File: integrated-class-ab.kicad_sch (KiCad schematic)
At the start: 1 part, among them U7 LT1794

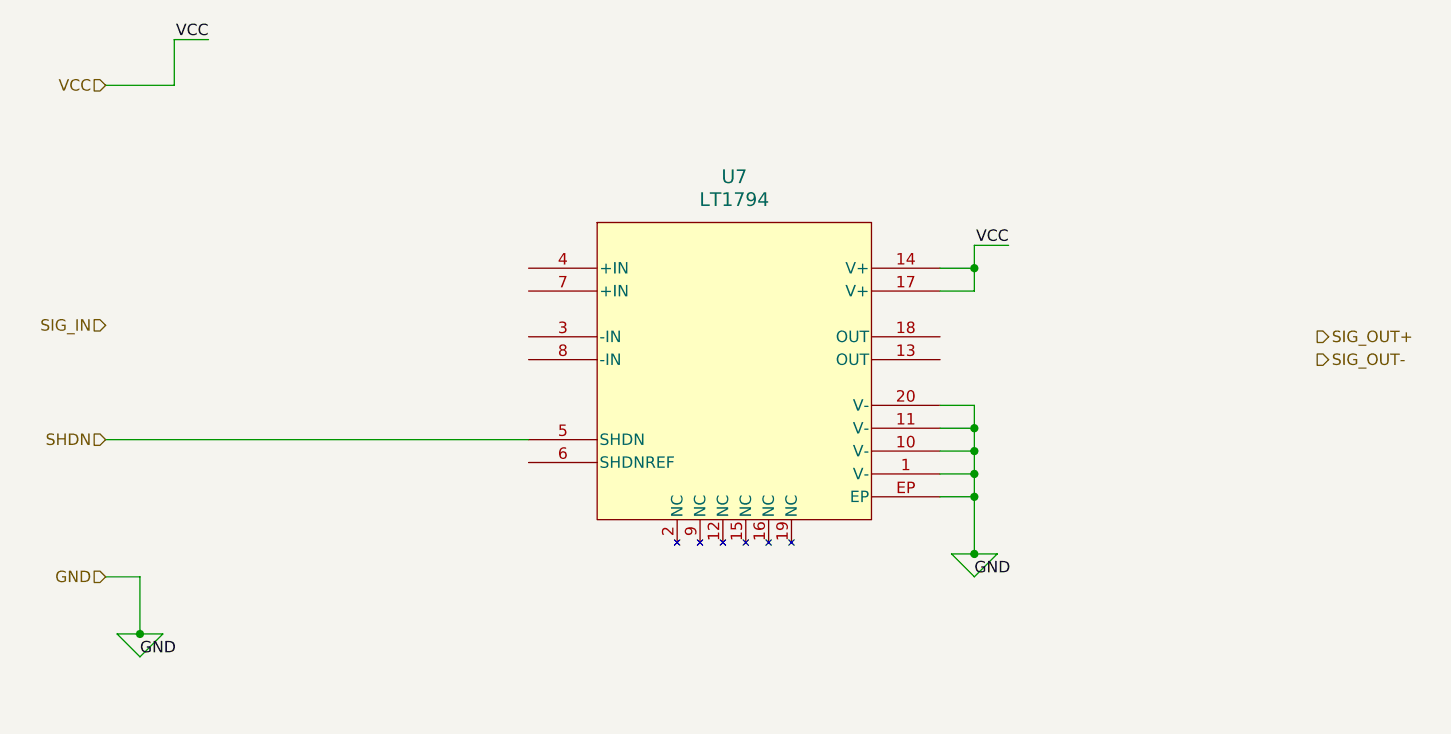
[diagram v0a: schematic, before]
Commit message: Added the pin headers to TX, working on a HV line driver design
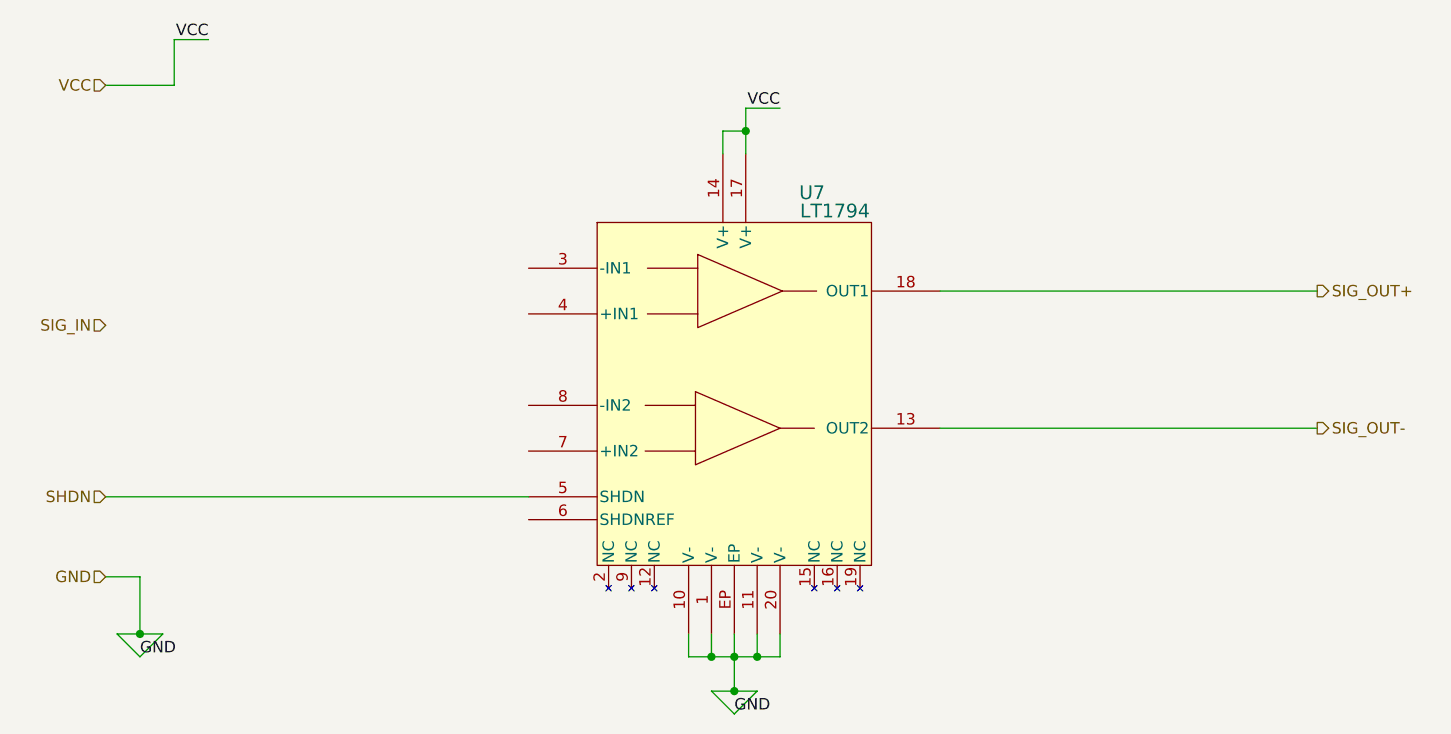
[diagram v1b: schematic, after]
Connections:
- net SIG_OUT+: now also U7.18 (OUT1)
- net SIG_OUT-: now also U7.13 (OUT2)
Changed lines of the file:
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@@
 	(paper "A4")
 	(junction
-		(at 176.53 96.52)
-		(diameter 0)
-		(color 0 0 0 0)
-	)
-	(junction
-		(at 176.53 102.87)
-		(diameter 0)
-		(color 0 0 0 0)
-	)
-	(junction
-		(at 176.53 93.98)
-		(diameter 0)
-		(color 0 0 0 0)
-	)
-	(junction
-		(at 176.53 91.44)
-		(diameter 0)
-		(color 0 0 0 0)
-	)
-	(junction
-		(at 176.53 88.9)
-		(diameter 0)
-		(color 0 0 0 0)
-	)
-	(junction
-		(at 176.53 71.12)
+		(at 147.32 114.3)
+		(diameter 0)
+		(color 0 0 0 0)
+	)
+	(junction
+		(at 149.86 118.11)
+		(diameter 0)
+		(color 0 0 0 0)
+	)
+	(junction
+		(at 149.86 114.3)
+		(diameter 0)
+		(color 0 0 0 0)
+	)
+	(junction
+		(at 151.13 55.88)
 		(diameter 0)
 		(color 0 0 0 0)
@@
 		(color 0 0 0 0)
 	)
-	(wire
-		(pts
-			(xy 176.53 96.52) (xy 172.72 96.52)
-		)
-		(stroke
-			(width 0)
-			(type default)
-		)
-	)
-	(wire
-		(pts
-			(xy 176.53 105.41) (xy 179.07 102.87)
+	(junction
+		(at 152.4 114.3)
+		(diameter 0)
+		(color 0 0 0 0)
+	)
+	(wire
+		(pts
+			(xy 144.78 111.76) (xy 144.78 114.3)
+		)
+		(stroke
+			(width 0)
+			(type default)
+		)
+	)
+	(wire
+		(pts
+			(xy 149.86 114.3) (xy 149.86 118.11)
+		)
+		(stroke
+			(width 0)
+			(type default)
+		)
+	)
+	(wire
+		(pts
+			(xy 149.86 120.65) (xy 152.4 118.11)
 		)
 		(stroke
@@
 	(wire
 		(pts
-			(xy 176.53 71.12) (xy 176.53 68.58)
+			(xy 151.13 55.88) (xy 151.13 53.34)
 		)
 		(stroke
@@
 	(wire
 		(pts
-			(xy 176.53 102.87) (xy 179.07 102.87)
-		)
-		(stroke
-			(width 0)
-			(type default)
-		)
-	)
-	(wire
-		(pts
-			(xy 176.53 93.98) (xy 176.53 91.44)
-		)
-		(stroke
-			(width 0)
-			(type default)
-		)
-	)
-	(wire
-		(pts
-			(xy 176.53 88.9) (xy 176.53 86.36)
+			(xy 149.86 118.11) (xy 152.4 118.11)
 		)
 		(stroke
@@
 	(wire
 		(pts
+			(xy 149.86 114.3) (xy 152.4 114.3)
+		)
+		(stroke
+			(width 0)
+			(type default)
+		)
+	)
+	(wire
+		(pts
+			(xy 144.78 114.3) (xy 147.32 114.3)
+		)
+		(stroke
+			(width 0)
+			(type default)
+		)
+	)
+	(wire
+		(pts
 			(xy 83.82 111.76) (xy 86.36 111.76)
 		)
@@
 	(wire
 		(pts
-			(xy 172.72 93.98) (xy 176.53 93.98)
-		)
-		(stroke
-			(width 0)
-			(type default)
-		)
-	)
-	(wire
-		(pts
-			(xy 172.72 91.44) (xy 176.53 91.44)
-		)
-		(stroke
-			(width 0)
-			(type default)
-		)
-	)
-	(wire
-		(pts
-			(xy 172.72 86.36) (xy 176.53 86.36)
-		)
-		(stroke
-			(width 0)
-			(type default)
-		)
-	)
-	(wire
-		(pts
-			(xy 172.72 71.12) (xy 176.53 71.12)
-		)
-		(stroke
-			(width 0)
-			(type default)
-		)
-	)
-	(wire
-		(pts
-			(xy 176.53 73.66) (xy 176.53 71.12)
-		)
-		(stroke
-			(width 0)
-			(type default)
-		)
-	)
-	(wire
-		(pts
-			(xy 176.53 91.44) (xy 176.53 88.9)
-		)
-		(stroke
-			(width 0)
-			(type default)
-		)
-	)
-	(wire
-		(pts
-			(xy 176.53 68.58) (xy 180.34 68.58)
+			(xy 147.32 114.3) (xy 149.86 114.3)
+		)
+		(stroke
+			(width 0)
+			(type default)
+		)
+	)
+	(wire
+		(pts
+			(xy 147.32 111.76) (xy 147.32 114.3)
+		)
+		(stroke
+			(width 0)
+			(type default)
+		)
+	)
+	(wire
+		(pts
+			(xy 151.13 58.42) (xy 151.13 55.88)
+		)
+		(stroke
+			(width 0)
+			(type default)
+		)
+	)
+	(wire
+		(pts
+			(xy 148.59 55.88) (xy 148.59 58.42)
+		)
+		(stroke
+			(width 0)
+			(type default)
+		)
+	)
+	(wire
+		(pts
+			(xy 151.13 53.34) (xy 154.94 53.34)
 		)
 		(stroke
@@
 	(wire
 		(pts
-			(xy 173.99 102.87) (xy 176.53 102.87)
+			(xy 152.4 111.76) (xy 152.4 114.3)
+		)
+		(stroke
+			(width 0)
+			(type default)
+		)
+	)
+	(wire
+		(pts
+			(xy 154.94 114.3) (xy 154.94 111.76)
+		)
+		(stroke
+			(width 0)
+			(type default)
+		)
+	)
+	(wire
+		(pts
+			(xy 147.32 118.11) (xy 149.86 118.11)
 		)
 		(stroke
@@
 	(wire
 		(pts
-			(xy 176.53 96.52) (xy 176.53 93.98)
-		)
-		(stroke
-			(width 0)
-			(type default)
-		)
-	)
-	(wire
-		(pts
-			(xy 176.53 96.52) (xy 176.53 102.87)
-		)
-		(stroke
-			(width 0)
-			(type default)
-		)
-	)
-	(wire
-		(pts
-			(xy 80.01 90.17) (xy 127 90.17)
-		)
-		(stroke
-			(width 0)
-			(type default)
-		)
-	)
-	(wire
-		(pts
-			(xy 172.72 88.9) (xy 176.53 88.9)
-		)
-		(stroke
-			(width 0)
-			(type default)
-		)
-	)
-	(wire
-		(pts
-			(xy 173.99 102.87) (xy 176.53 105.41)
+			(xy 172.72 88.9) (xy 214.63 88.9)
+		)
+		(stroke
+			(width 0)
+			(type default)
+		)
+	)
+	(wire
+		(pts
+			(xy 149.86 111.76) (xy 149.86 114.3)
+		)
+		(stroke
+			(width 0)
+			(type default)
+		)
+	)
+	(wire
+		(pts
+			(xy 152.4 114.3) (xy 154.94 114.3)
+		)
+		(stroke
+			(width 0)
+			(type default)
+		)
+	)
+	(wire
+		(pts
+			(xy 148.59 55.88) (xy 151.13 55.88)
+		)
+		(stroke
+			(width 0)
+			(type default)
+		)
+	)
+	(wire
+		(pts
+			(xy 80.01 96.52) (xy 127 96.52)
+		)
+		(stroke
+			(width 0)
+			(type default)
+		)
+	)
+	(wire
+		(pts
+			(xy 147.32 118.11) (xy 149.86 120.65)
 		)
 		(stroke
@@
 	(wire
 		(pts
-			(xy 172.72 73.66) (xy 176.53 73.66)
+			(xy 172.72 73.66) (xy 214.63 73.66)
 		)
 		(stroke
@@
 	)
 	(label "GND"
-		(at 176.53 105.41 0)
+		(at 149.86 120.65 0)
 		(effects
 			(font
@@
 	)
 	(label "VCC"
-		(at 180.34 68.58 180)
+		(at 154.94 53.34 180)
 		(effects
 			(font
@@
 	(hierarchical_label "SIG_OUT+"
 		(shape output)
-		(at 214.63 78.74 0)
+		(at 214.63 73.66 0)
 		(effects
 			(font
@@
 	(hierarchical_label "SHDN"
 		(shape input)
-		(at 80.01 90.17 180)
+		(at 80.01 96.52 180)
 		(effects
 			(font
@@
 	(hierarchical_label "SIG_OUT-"
 		(shape output)
-		(at 214.63 81.28 0)
+		(at 214.63 88.9 0)
 		(effects
 			(font
@@
 		(on_board yes)
 		(dnp no)
-		(fields_autoplaced yes)
 		(property "Reference" "U7"
-			(at 149.86 60.96 0)
+			(at 158.496 62.738 0)
 			(effects
 				(font
@@
 		)
 		(property "Value" "LT1794"
-			(at 149.86 63.5 0)
+			(at 161.036 64.77 0)
 			(effects
 				(font

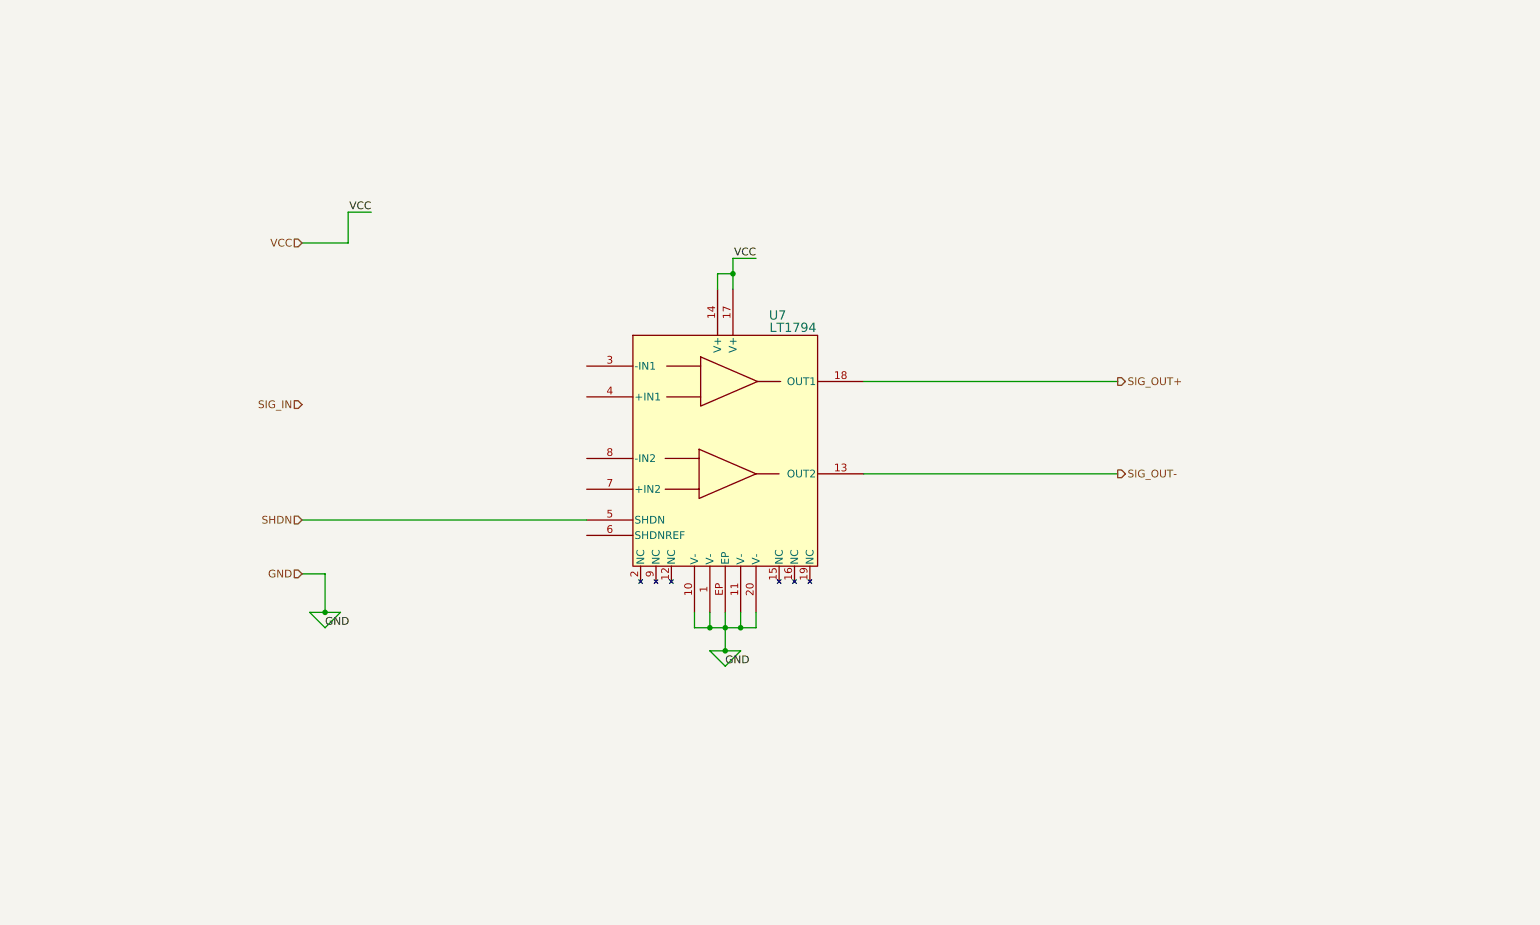
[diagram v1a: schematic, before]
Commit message: Created DAC single-ended to double-ended pre stage for TX path
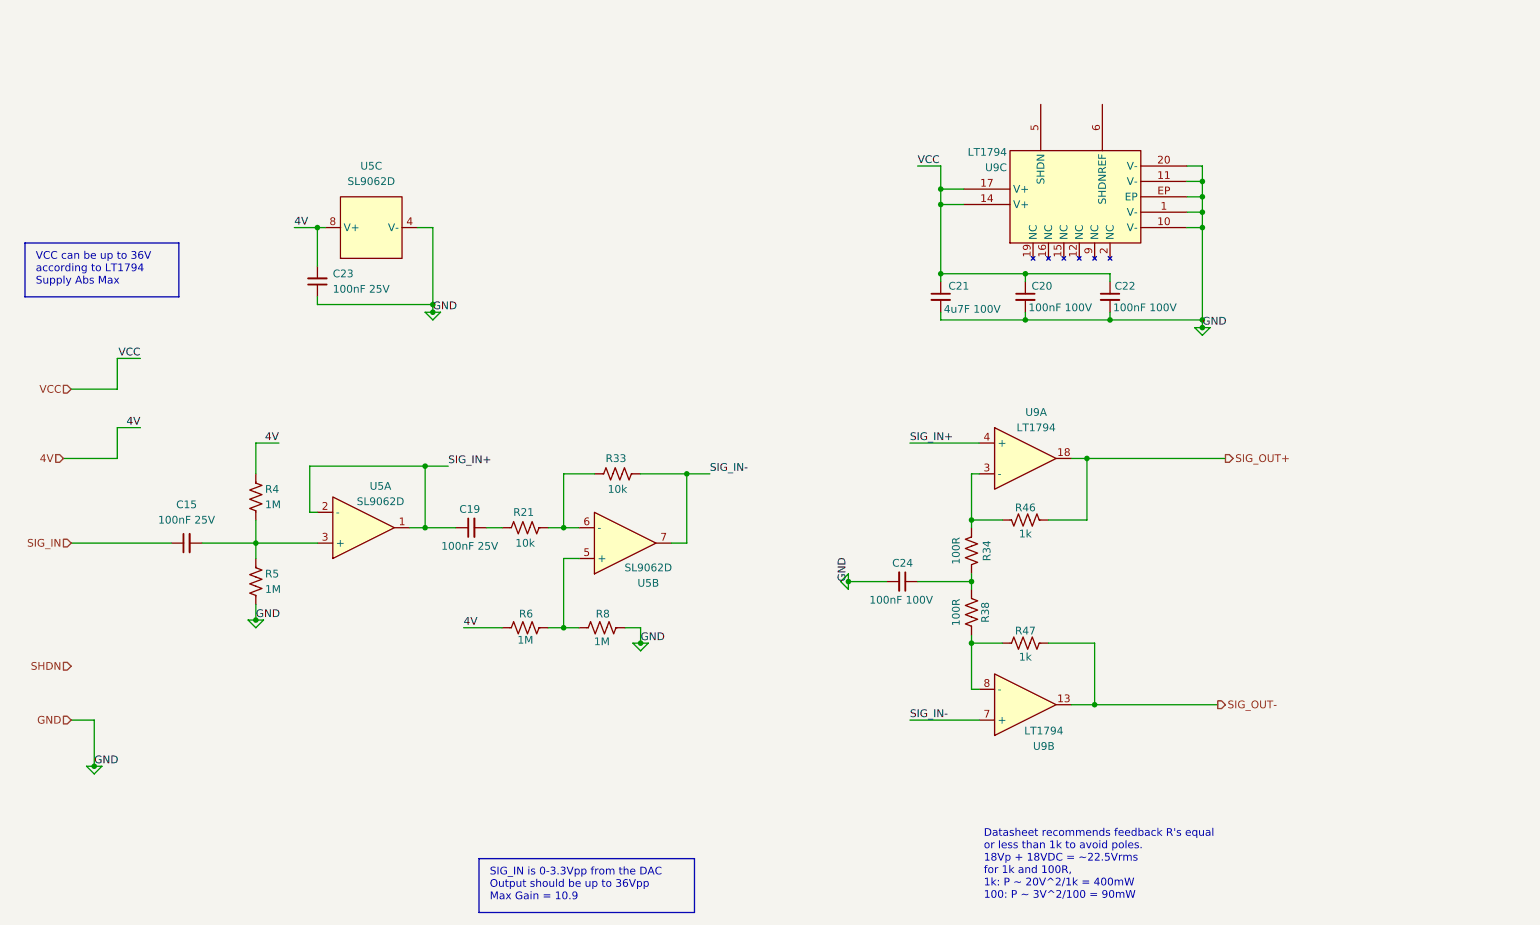
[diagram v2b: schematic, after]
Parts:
- removed U7: LT1794, BR_SOP:TSSOP-20_FE_6.4x6.4mm_EP4.95x2.74mm, symbol BR_IC_Audio:LT1794CFE-PBF
- added C15, C19, C23: 100nF 25V, BR_Passives:C_0201_0603Metric-minimized, symbol BR_Capacitors_0201:C_0201_100nF_25V_X7R_10%
- added C20, C22, C24: 100nF 100V, BR_Passives:C_0402_1005Metric-minimized, symbol BR_Capacitors_0402:C_0402_100nF_100V_X5R_20%
- added C21: 4u7F 100V, BR_Passives:C_1206_3216Metric-minimized, symbol BR_Capacitors_1206:C_1206_4u7F_100V_X7S_10%
- added R21, R33: 10k, BR_Passives:R_0201_0603Metric-minimized, symbol BR_Resistors_0201:R_0201_10k
- added R34, R38: 100R, BR_Passives:R_0603_1608Metric, symbol BR_Resistors_0603:R_0603_100R
- added R4, R5, R6, R8: 1M, BR_Passives:R_0201_0603Metric-minimized, symbol BR_Resistors_0201:R_0201_1M
- added R46, R47: 1k, BR_Passives:C_1210_3225Metric-minimized, symbol BR_Resistors_1210:R_1210_1k
- added U5: SL9062D, BR_SOT:SOT-23-8, symbol BR_IC_Op_Amps:SL9062D
- added U9: LT1794, BR_SOP:TSSOP-20_FE_6.4x6.4mm_EP4.95x2.74mm, symbol BR_IC_Audio:LT1794CFE-PBF
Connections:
- net GND: now also C20.2, C21.2, C22.2, C23.1, C24.2, R5.2, R8.2, U5.4 (V-), U9.1 (V-), U9.10 (V-), U9.11 (V-), U9.20 (V-), U9.EP
- net SIG_IN: now also C15.1
- net SIG_OUT+: now also R46.1, U9.18
- net SIG_OUT-: now also R47.2, U9.13
- net VCC: now also C20.1, C21.1, C22.1, U9.14 (V+), U9.17 (V+)
- new net: R38.2, R47.1, U9.8 (-)
- new net: C24.1, R34.1, R38.1
- new net: R34.2, R46.2, U9.3 (-)
- new net: R6.2, R8.1, U5.5 (+)
- new net: C15.2, R4.2, R5.1, U5.3 (+)
- new net: R21.2, R33.1, U5.6 (-)
- new net: C19.2, R21.1
- new net 4V: C23.2, R4.1, R6.1, U5.8 (V+)
- new net SIG_IN+: C19.1, U5.1, U5.2 (-), U9.4 (+)
- new net SIG_IN-: R33.2, U5.7, U9.7 (+)
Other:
- note added: "Datasheet recommends feedback R's equal or less than 1k to avoid poles. 18Vp + 18VDC = ~22.5Vrms for 1k and 100R, 1k: P ~ 20V^2/1k = 400mW 100: P ~ 3V^2/100 = 90mW"
- note added: "SIG_IN is 0-3.3Vpp from the DAC Output should be up to 36Vpp Max Gain = 10.9"
- note added: "VCC can be up to 36V according to LT1794 Supply Abs Max"

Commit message: shit on a shit stick
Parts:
- added C25, C26: 470nF 100V, BR_Passives:C_0805_2012Metric-minimized, symbol BR_Capacitors_0805:C_0805_470nF_100V_X7R_10%
- added C27, C29: 100nF 100V, BR_Passives:C_0402_1005Metric-minimized, symbol BR_Capacitors_0402:C_0402_100nF_100V_X5R_20%
- added R50, R51, R52, R53, R54, R55: 100k, BR_Passives:R_0201_0603Metric-minimized, symbol BR_Resistors_0201:R_0201_100k
- R5, R8: value 1M -> 750k; footprint BR_Passives:R_0201_0603Metric-minimized -> BR_Passives:C_0201_0603Metric-minimized; symbol BR_Resistors_0201:R_0201_1M -> BR_Resistors_0201:R_0201_750k_AEC-Q200; BRE Number BRE-001254 -> BRE-001258; JLCPCB Part Num C295786 -> C5942591; Manufacturer Part Num RC0201FR-071ML -> AF0201FR-07750KL; Supplier 1 (none) -> DigiKey; Supplier 2 (none) -> Mouser; Supplier 3 (none) -> JLCPCB; Supplier Part Num 1 (none) -> RC0201DR-07681RL-ND; Supplier Part Num 2 (none) -> 603-RC0201DR-07681RL; Supplier Part Num 3 (none) -> C851780
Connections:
- net GND: now also R50.2, R51.2, R53.2, R55.2
- net SIG_IN+: now also C27.2; no longer U9.4 (+)
- net SIG_IN-: now also C29.2; no longer U9.7 (+)
- net SIG_OUT+: now also C25.2, R51.1; no longer R46.1, U9.18
- net SIG_OUT-: now also C26.2, R50.1; no longer R47.2, U9.13
- net VCC: now also R52.1, R54.1
- new net: C26.1, R47.2, U9.13
- new net: C27.1, R52.2, R53.1, U9.4 (+)
- new net: C25.1, R46.1, U9.18
- new net: C29.1, R54.2, R55.1, U9.7 (+)
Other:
- moved on the sheet: C24, R34, R38, R46, R47, U9A, U9B

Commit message: Added current sense and shutdown/bias current pin control to LT1794 line driver
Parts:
- added C37: 100nF 25V, BR_Passives:C_0201_0603Metric-minimized, symbol BR_Capacitors_0201:C_0201_100nF_25V_X7R_10%
- added R56: 50k, BR_Passives:RES-ADJ-SMD_3P-L3.8-W3.7_VGF39NCHXT, symbol BR_Passives_misc:POT_50k_VGF39NCHXT-B503
- added R57: 10mR, BR_Passives:R_0805_2012Metric, symbol BR_Resistors_0805:R_0805_10mR
- added TP55: TP_SQUARE_TH_500um, POT1, symbol BR_Virtual_Parts:TP_SQUARE_TH_1mm
- added TP56: POT2, BR_Virtual_Parts:TP_SQUARE_TH_1mm, symbol BR_Virtual_Parts:TP_SQUARE_TH_1mm
- added U10: CSA230PASOT235, BR_SOT:SOT-23-5_mini, symbol BR_Sensors:Current_Sense_CSA230PASOT235
- R5, R8: value 750k -> 1M; footprint BR_Passives:C_0201_0603Metric-minimized -> BR_Passives:R_0201_0603Metric-minimized; symbol BR_Resistors_0201:R_0201_750k_AEC-Q200 -> BR_Resistors_0201:R_0201_1M; BRE Number BRE-001258 -> BRE-001254; JLCPCB Part Num C5942591 -> C295786; Manufacturer Part Num AF0201FR-07750KL -> RC0201FR-071ML
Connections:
- net 4V: now also C37.1, U10.3 (VDD)
- net GND: now also U9.6 (SHDNREF), C37.2, U10.1 (GND)
- net SIG_OUT+: now also R57.2, U10.4 (RS–); no longer C25.2, R51.1
- net TX_EN: now also R56.3
- net at U9.5 (SHDN): now also R56.2 (W), TP56.1
- new net: C25.2, R51.1, R57.1, U10.5 (RS+)
- new net: R56.1, TP55.1
- new net I_SENSE: U10.2 (OUT)
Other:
- note added: "10mV/1A over 10mR R57 100V/1V from I Sense Amp Therefore, 1V/1A"
- note added: "Measure resistance across test points to get actual R = 50k-{measured}"
- note added: "SHDN pin also controls Class AB bias current. Ibias = 25.6*(TX_EN - 1.2V)/(R + 2k) When TX_EN High, pot gives range of 1mA-27mA"

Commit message: rewiring STM32H563
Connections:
- net 4V renamed 5V
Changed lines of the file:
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@@
 		)
 	)
-	(label "4V"
+	(label "5V"
 		(at 76.2 83.82 180)
 		(effects
@@
 		)
 	)
-	(label "4V"
+	(label "5V"
 		(at 53.34 81.28 180)
 		(effects
@@
 		)
 	)
-	(label "4V"
+	(label "5V"
 		(at 261.62 93.98 180)
 		(effects
@@
 		)
 	)
-	(label "4V"
+	(label "5V"
 		(at 78.74 48.26 0)
 		(effects
@@
 		)
 	)
-	(label "4V"
+	(label "5V"
 		(at 106.68 114.3 0)
 		(effects
@@
 		)
 	)
-	(hierarchical_label "4V"
+	(hierarchical_label "5V"
 		(shape input)
 		(at 40.64 86.36 180)
